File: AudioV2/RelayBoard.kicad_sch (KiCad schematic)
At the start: 10 parts, among them K1 AZ850 CH1 audio, K2 AZ850 CH1 pwr, K3 AZ850 CH2 audio, K4 AZ850 CH2 pwr, K5 AZ850 CH3 audio, U1 MCP23017 addr0x20, U2 ULN2803A

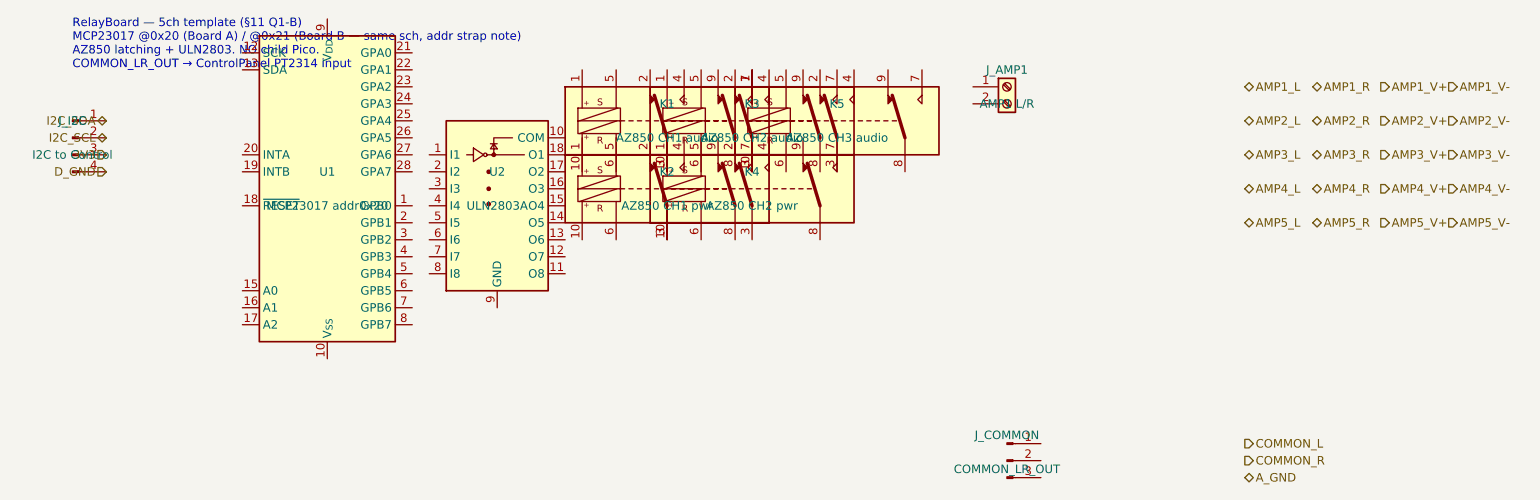
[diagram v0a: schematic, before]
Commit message: AudioV2: Power PD端子整理とエージェント引き継ぎ更新
PowerModule に J201/J202/J203 を揃え、PWR SW は ControlPanel に戻す。
AGENT_HANDOFF / WIRING に現状トポロジと PD A/B メモを残し、クラウド同期用に main へ載せる。

Co-authored-by: Cursor <cursoragent@cursor.com>
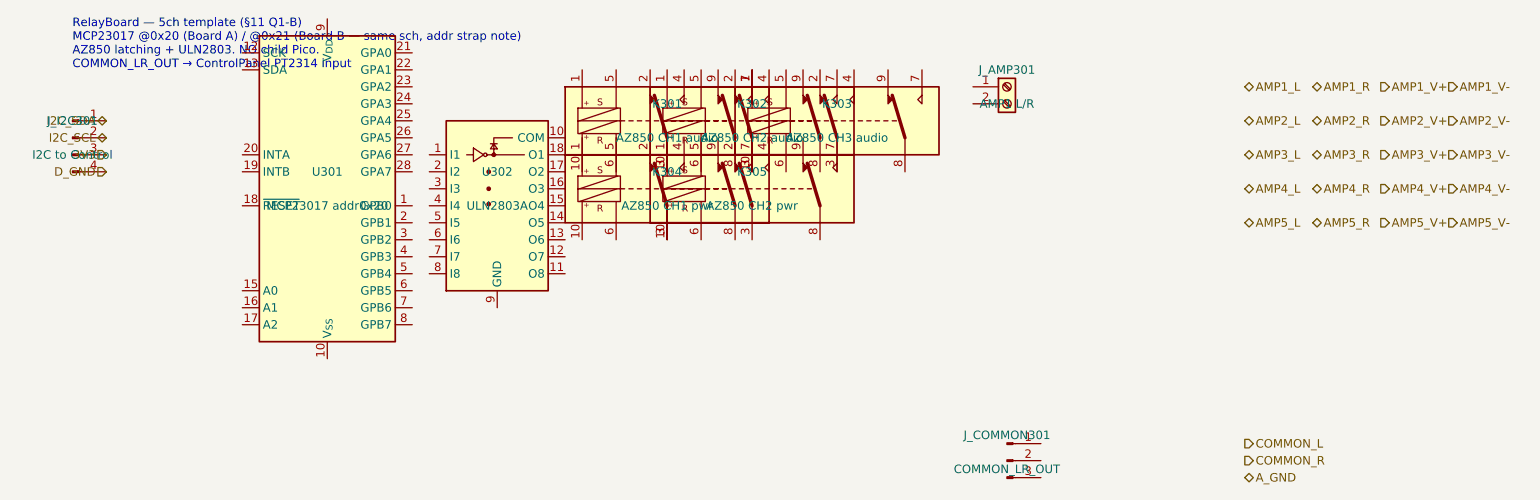
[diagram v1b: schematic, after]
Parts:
- renumbered J_AMP1 to J_AMP301, J_COMMON to J_COMMON301, J_I2C to J_I2C301, K1 to K301, K3 to K302, K5 to K303, K2 to K304, K4 to K305, U1 to U301, U2 to U302

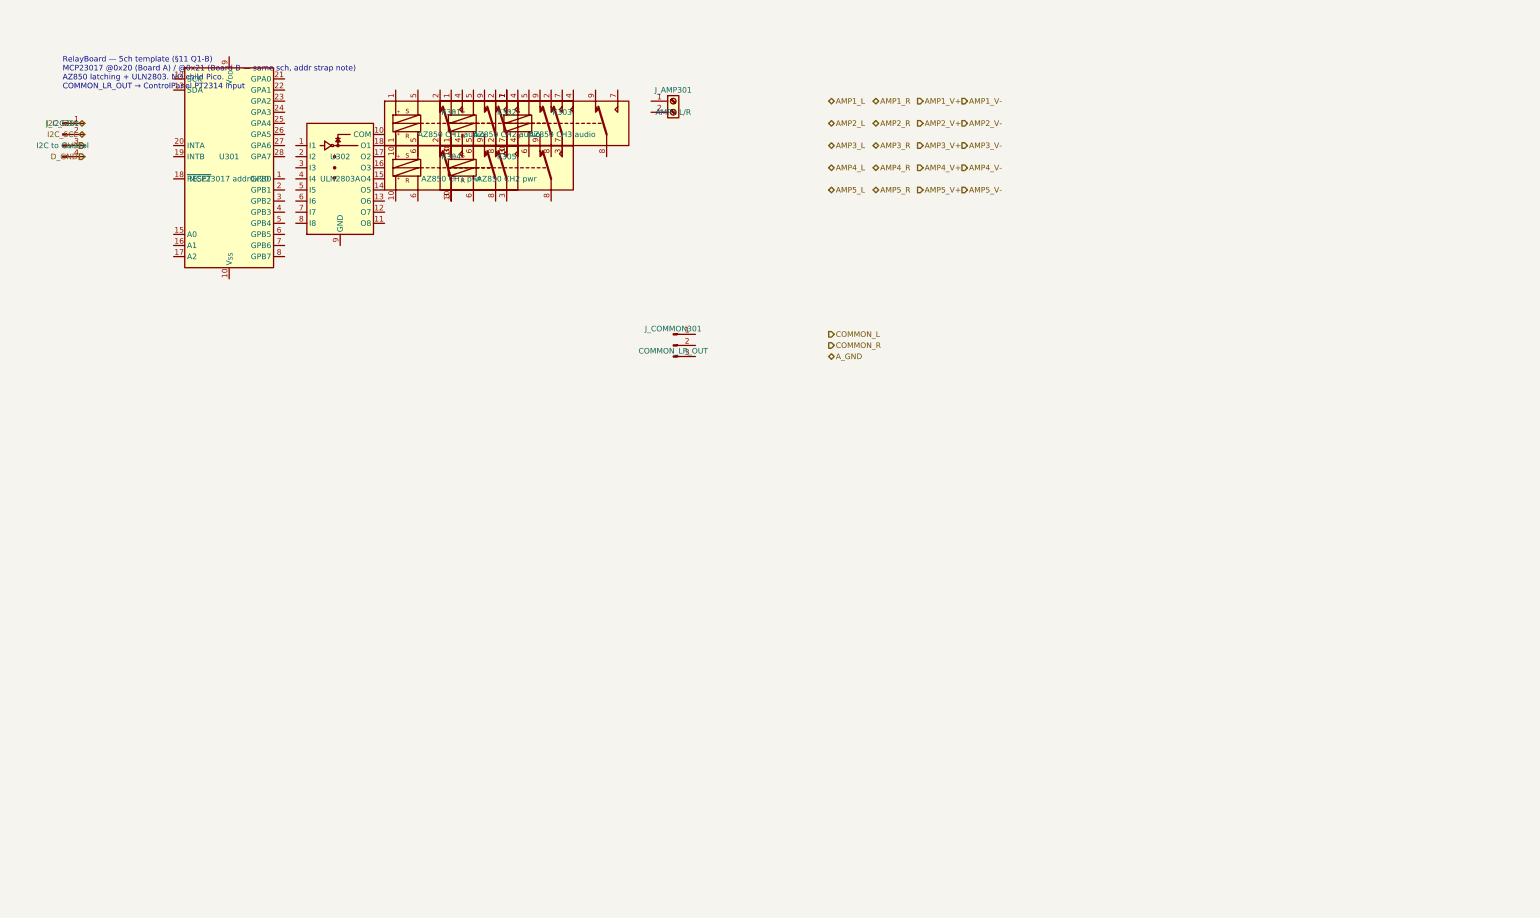
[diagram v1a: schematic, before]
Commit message: AudioV2: Amp再版とRelayBoard本配線、番地ストラップを0Ω化
高速オペアンプを差せるようAmpをバルク対応で再版した（ゲイン2＝20k/20k、
±12V、100µF/rail + 100nF + 1nF、DIP-8ソケット）。親には代表1シートだけ置き、
物理は同一仕様×10製造とする。PCBは既存基板の端子・4穴を維持したまま上辺を
15mm拡張してバルクを載せた。

RelayBoardは未給電Ampへ信号を印加しないよう、Amp入力と±12Vを同一の
SET/RESETで同時切替する構成で本配線した。番地はA1/A0の0Ωストラップで
0x20–0x23を選び、1枚のPCB設計を最大4枚に使い回す。SolderJumperは
FPが1.3mmピッチで0Ωチップが載らないため1206パッドに変更した。
プルダウン10kΩはジャンパ後段に置き常時実装（手前分岐だと未実装時に
A0/A1が浮く）。

ERC 207→56。Power/Output/Amp/Relay A・B は0件で、残りはControlの
未使用ピンと親の箱外ラベル。AmpのPCB DRCは電気エラー0・未配線0。

レビュー指摘（IC直近パスコン、AZ850のset voltage余裕、A0/A1ネット無名）は
未対応でAGENT_HANDOFF §2.7に記録。addr_strapのスクリプト側は現図と
非同期なので、同期までwire_circuit_design.py relayを回さない。

Co-authored-by: Cursor <cursoragent@cursor.com>
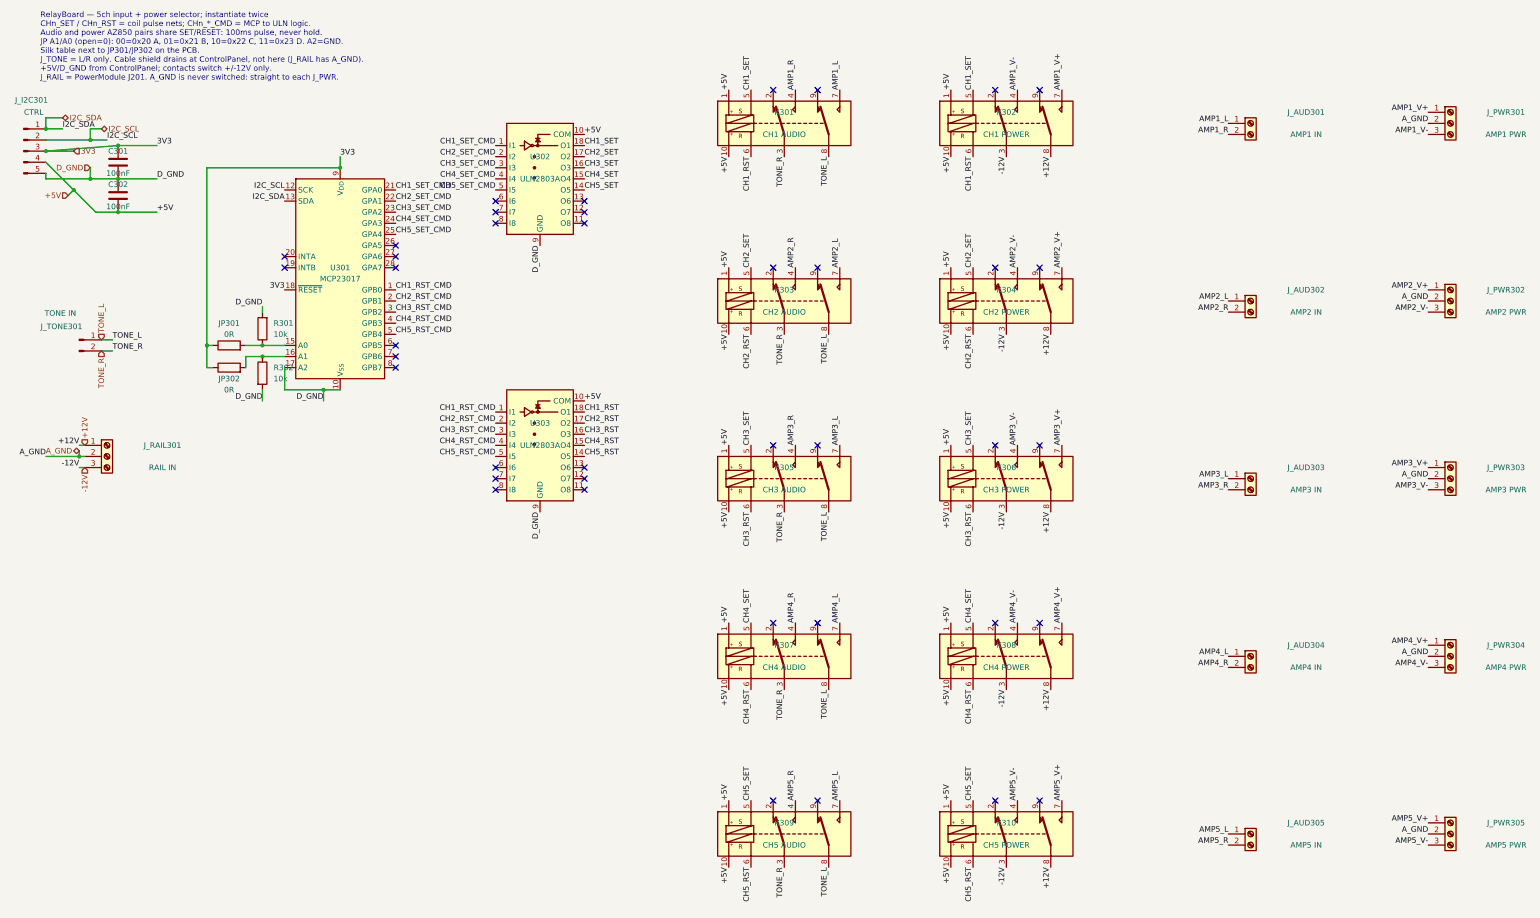
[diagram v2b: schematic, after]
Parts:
- removed J_AMP301: AMP1 L/R, symbol Connector:Screw_Terminal_01x02
- removed J_COMMON301: COMMON_LR_OUT, symbol Connector:Conn_01x03_Pin
- removed J_I2C301: I2C to Control, symbol Connector:Conn_01x04_Pin
- added C301, C302: 100nF, symbol Device:C
- added JP301, JP302: 0R, Resistor_SMD:R_1206_3216Metric_Pad1.30x1.75mm_HandSolder, symbol Device:R
- added J_AUD301: AMP1 IN, symbol Connector:Screw_Terminal_01x02
- added J_AUD302: AMP2 IN, symbol Connector:Screw_Terminal_01x02
- added J_AUD303: AMP3 IN, symbol Connector:Screw_Terminal_01x02
- added J_AUD304: AMP4 IN, symbol Connector:Screw_Terminal_01x02
- added J_AUD305: AMP5 IN, symbol Connector:Screw_Terminal_01x02
- added J_I2C301: CTRL, symbol Connector:Conn_01x05_Pin
- added J_PWR301: AMP1 PWR, symbol Connector:Screw_Terminal_01x03
- added J_PWR302: AMP2 PWR, symbol Connector:Screw_Terminal_01x03
- added J_PWR303: AMP3 PWR, symbol Connector:Screw_Terminal_01x03
- added J_PWR304: AMP4 PWR, symbol Connector:Screw_Terminal_01x03
- added J_PWR305: AMP5 PWR, symbol Connector:Screw_Terminal_01x03
- added J_RAIL301: RAIL IN, symbol Connector:Screw_Terminal_01x03
- added J_TONE301: TONE IN, symbol Connector:Conn_01x02_Pin
- added K306: CH3 POWER, symbol Relay:AZ850P2-x
- added K307: CH4 AUDIO, symbol Relay:AZ850P2-x
- added K308: CH4 POWER, symbol Relay:AZ850P2-x
- added K309: CH5 AUDIO, symbol Relay:AZ850P2-x
- added K310: CH5 POWER, symbol Relay:AZ850P2-x
- added R301, R302: 10k, Resistor_SMD:R_1206_3216Metric_Pad1.30x1.75mm_HandSolder, symbol Device:R
- added U303: ULN2803A, symbol Transistor_Array:ULN2803A
- K301: value AZ850 CH1 audio -> CH1 AUDIO
- K302: value AZ850 CH2 audio -> CH1 POWER
- K303: value AZ850 CH3 audio -> CH2 AUDIO
- K304: value AZ850 CH1 pwr -> CH2 POWER
- K305: value AZ850 CH2 pwr -> CH3 AUDIO
- U301: value MCP23017 addr0x20 -> MCP23017; Addr 0x20 A / 0x21 B -> JP A1/A0 → 0x20-0x23; A2=0
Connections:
- net 3V3: now also U301.18 (~{RESET}), U301.9 (V_{DD}), C301.1, JP301.1, JP302.1, J_I2C301.3 (Pin_3)
- net AMP1_L: now also K301.7, J_AUD301.1 (Pin_1)
- net AMP1_R: now also K301.4, J_AUD301.2 (Pin_2)
- net AMP1_V+: now also K302.7, J_PWR301.1 (Pin_1)
- net AMP1_V-: now also K302.4, J_PWR301.3 (Pin_3)
- net AMP2_L: now also K303.7, J_AUD302.1 (Pin_1)
- net AMP2_R: now also K303.4, J_AUD302.2 (Pin_2)
- net AMP2_V+: now also K304.7, J_PWR302.1 (Pin_1)
- net AMP2_V-: now also K304.4, J_PWR302.3 (Pin_3)
- net AMP3_L: now also K305.7, J_AUD303.1 (Pin_1)
- net AMP3_R: now also K305.4, J_AUD303.2 (Pin_2)
- net AMP3_V+: now also J_PWR303.1 (Pin_1), K306.7
- net AMP3_V-: now also J_PWR303.3 (Pin_3), K306.4
- net AMP4_L: now also J_AUD304.1 (Pin_1), K307.7
- net AMP4_R: now also J_AUD304.2 (Pin_2), K307.4
- net AMP4_V+: now also J_PWR304.1 (Pin_1), K308.7
- net AMP4_V-: now also J_PWR304.3 (Pin_3), K308.4
- net AMP5_L: now also J_AUD305.1 (Pin_1), K309.7
- net AMP5_R: now also J_AUD305.2 (Pin_2), K309.4
- net AMP5_V+: now also J_PWR305.1 (Pin_1), K310.7
- net AMP5_V-: now also J_PWR305.3 (Pin_3), K310.4
- net A_GND: now also J_PWR301.2 (Pin_2), J_PWR302.2 (Pin_2), J_PWR303.2 (Pin_2), J_PWR304.2 (Pin_2), J_PWR305.2 (Pin_2), J_RAIL301.2 (Pin_2)
- net D_GND: now also U301.10 (V_{SS}), U301.17 (A2), U302.9 (GND), C301.2, C302.1, J_I2C301.5 (Pin_5), R301.2, R302.2, U303.9 (GND)
- net I2C_SCL: now also U301.12 (SCK), J_I2C301.2 (Pin_2)
- net I2C_SDA: now also U301.13 (SDA), J_I2C301.1 (Pin_1)
- net +5V: now reaches K304.1
- net +5V: now also K301.1, K301.10, K302.1, K302.10, K303.1, K303.10, K304.10, K305.1, K305.10, U302.10 (COM), C302.2, J_I2C301.4 (Pin_4), K306.1, K306.10, K307.1, K307.10, K308.1, K308.10, K309.1, K309.10, K310.1, K310.10, U303.10 (COM)
- net -12V: now reaches K304.3
- net -12V: now also K302.3, J_RAIL301.3 (Pin_3), K306.3, K308.3, K310.3; no longer K305.10
- net CH2_SET: now reaches K304.5
- net CH2_SET: now also K303.5, U302.17 (O2)
- net CH2_RST: now reaches K304.6
- net CH2_RST: now also K303.6, U303.17 (O2)
- net +12V: now reaches K304.8
- net +12V: now also K302.8, J_RAIL301.1 (Pin_1), K306.8, K308.8, K310.8
- net TONE_R: now reaches K303.3
- net TONE_R: now also K301.3, K305.3, J_TONE301.2 (Pin_2), K307.3, K309.3
- net TONE_L: now reaches K303.8
- net TONE_L: now also K301.8, K305.8, J_TONE301.1 (Pin_1), K307.8, K309.8
- net CH1_RST_CMD: now reaches U301.1 (GPB0)
- net CH1_RST_CMD: now also U303.1 (I1)
- net at U301.15 (A0): now also JP301.2, R301.1
- net at U301.16 (A1): now also JP302.2, R302.1
- net CH2_RST_CMD: now reaches U301.2 (GPB1)
- net CH2_RST_CMD: now also U303.2 (I2)
- net CH1_SET_CMD: now reaches U301.21 (GPA0)
- net CH1_SET_CMD: now also U302.1 (I1)
- net CH2_SET_CMD: now reaches U301.22 (GPA1)
- net CH2_SET_CMD: now also U302.2 (I2)
- net CH3_SET_CMD: now reaches U301.23 (GPA2)
- net CH3_SET_CMD: now also U302.3 (I3)
- net CH4_SET_CMD: now reaches U301.24 (GPA3)
- net CH4_SET_CMD: now also U302.4 (I4)
- net CH5_SET_CMD: now reaches U301.25 (GPA4)
- net CH5_SET_CMD: now also U302.5 (I5)
- net CH3_RST_CMD: now reaches U301.3 (GPB2)
- net CH3_RST_CMD: now also U303.3 (I3)
- net CH4_RST_CMD: now reaches U301.4 (GPB3)
- net CH4_RST_CMD: now also U303.4 (I4)
- net CH5_RST_CMD: now reaches U301.5 (GPB4)
- net CH5_RST_CMD: now also U303.5 (I5)
- net CH1_SET: now reaches K301.5
- net CH1_SET: now also K302.5, U302.18 (O1)
- net CH1_RST: now reaches K301.6
- net CH1_RST: now also K302.6, U303.18 (O1)
- net CH3_SET: now reaches K305.5
- net CH3_SET: now also U302.16 (O3), K306.5
- net CH3_RST: now reaches K305.6
- net CH3_RST: now also K306.6, U303.16 (O3)
- net CH5_SET: now reaches U302.14 (O5)
- net CH5_SET: now also K309.5, K310.5
- net CH4_SET: now reaches U302.15 (O4)
- net CH4_SET: now also K307.5, K308.5
- new net CH4_RST: K307.6, K308.6, U303.15 (O4)
- new net CH5_RST: K309.6, K310.6, U303.14 (O5)
- no-connect marks 0 -> 40
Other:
- note added: "RelayBoard — 5ch input + power selector; instantiate twice CHn_SET / CHn_RST = coil pulse nets; CHn_*_CMD = MCP to ULN logic. Audio and power AZ850 pairs share SET/RESET: 100ms pulse, never hold. JP A1/A0 (open=0): 00=0x20 A, 01=0x21 B, 10=0x22 C, 11=0x23 D. A2=GND. Silk table next to JP301/JP302 on the PCB. J_TONE = L/R only. Cable shield drains at ControlPanel, not here (J_RAIL has A_GND). +5V/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"
- note removed: "RelayBoard — 5ch template (§11 Q1-B) MCP23017 @0x20 (Board A) / @0x21 (Board B — same sch, addr strap note) AZ850 latching + ULN2803. NO child Pico. COMMON_LR_OUT → ControlPanel PT2314 input"
